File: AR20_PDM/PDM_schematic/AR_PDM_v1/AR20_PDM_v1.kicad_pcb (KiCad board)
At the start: 2 copper layers, 118 x 112 mm, 238 parts, among them J1 S_T_?, J2 1-776163-1, K1 DIPxx-1Cxx-51x, K2 DIPxx-1Cxx-51x, P1 B4B-PH-SM4-TB, Q1 BTS50025-1TAD, Q10 N_FET, Q11 N_FET, Q12 N_FET, Q13 N_FET, Q14 N_FET, Q15 N_FET, Q16 N_FET, Q17 N_FET, Q18 N_FET, Q2 BTS50025-1TAD, Q3 BTS50025-1TAD, Q4 N_FET, Q5 BTS50025-1TAD, Q6 BTS50025-1TAD, Q7 BTS50025-1TAD, Q8 BTS50025-1TAD, Q9 N_FET, SW1 SW_DIP_x07, U1 ACM_2020, U10 Fet-P, U11 Fet-P, U12 Fet-P, U13 Fet-P, U14 Fet-P, U15 Fet-P, U16 Fet-P, U17 Fet-P, U18 Fet-P, U19 Fet-P, U2 INA233, U20 Fet-P, U21 Fet-P, U22 Fet-P, U23 Fet-P, U24 Fet-P, U25 Fet-P, U26 Fet-P, U27 Fet-P, U28 Fet-P, U29 INA233, U3 INA233, U30 INA233, U31 INA233, U4 INA233, U5 INA233, U6 INA233, U7 INA233, U8 INA233, U9 TCA6424ARGJR

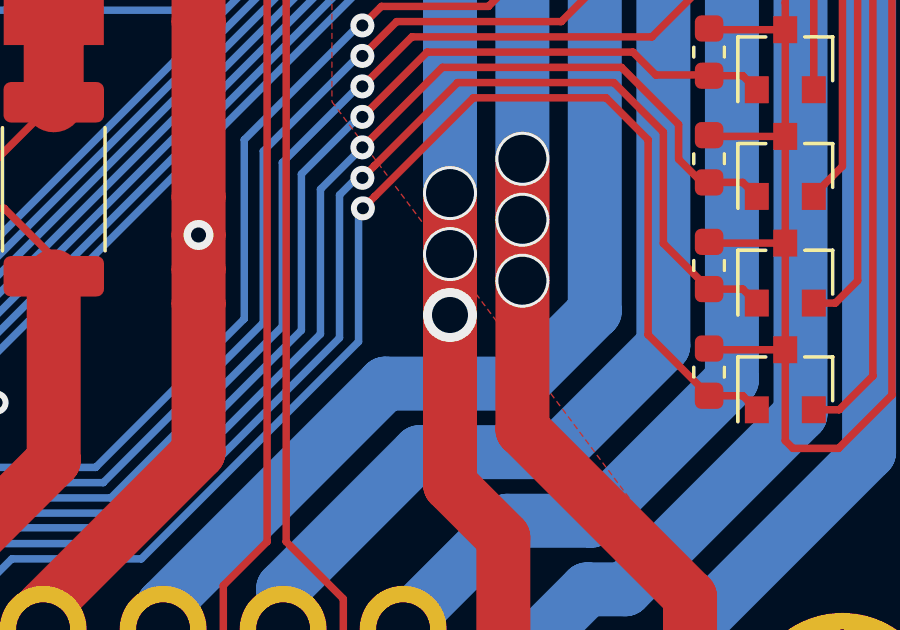
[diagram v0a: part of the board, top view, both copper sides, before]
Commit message: Generated new gerberfile, with forgotten solder mask
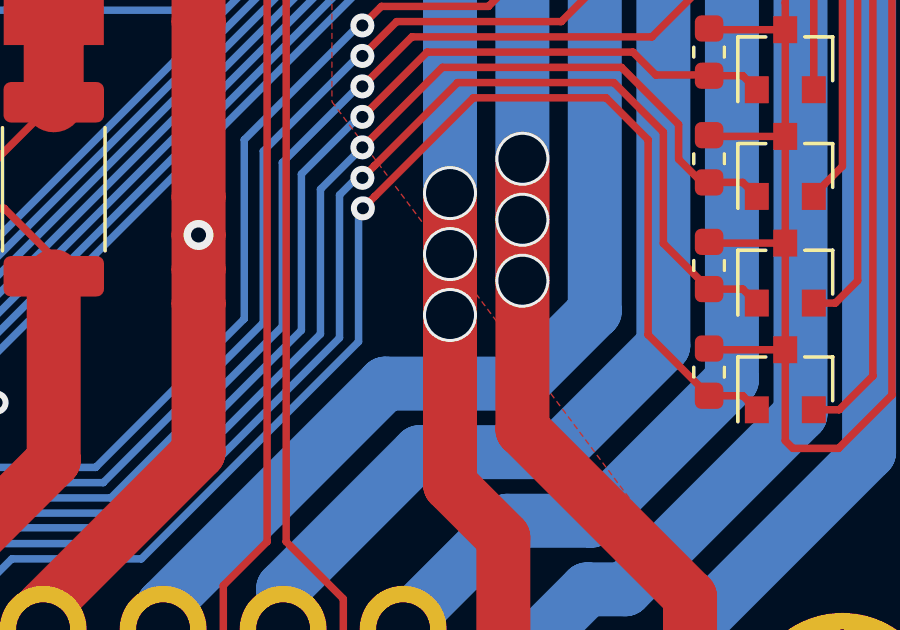
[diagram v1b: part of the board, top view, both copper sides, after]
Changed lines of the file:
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@@
     (visible_elements 7FFFFFFF)
     (pcbplotparams
-      (layerselection 0x0103c_ffffffff)
-      (usegerberextensions false)
+      (layerselection 0x010fc_ffffffff)
+      (usegerberextensions true)
       (usegerberattributes false)
       (usegerberadvancedattributes false)
@@
       (psnegative false)
       (psa4output false)
-      (plotreference false)
-      (plotvalue false)
+      (plotreference true)
+      (plotvalue true)
       (plotinvisibletext false)
       (padsonsilk false)
@@
   (segment (start 131.064 94.594) (end 134.747 98.277) (width 1.8) (layer B.Cu) (net 63))
   (segment (start 134.747 119.634) (end 134.747 124.206) (width 1.8) (layer B.Cu) (net 63))
-  (via (at 134.747 124.206) (size 1.8) (drill 1.2) (layers F.Cu B.Cu) (net 63) (status 1000000))
+  (via (at 134.747 124.206) (size 1.8) (drill 1.6) (layers F.Cu B.Cu) (net 63) (status 1000000))
   (segment (start 138.811 146.177) (end 140.97 146.177) (width 1.8) (layer F.Cu) (net 64))
   (via (at 138.811 146.177) (size 1.8) (drill 1.6) (layers F.Cu B.Cu) (net 64))

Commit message: Major redesign. schematics completed, PCB work in progress
-TODO : A proper changelog file. Where all changes will apear 
- Redesigned schematics to accommodate errors in the improvement list
- More detail in ALPHA improvement list
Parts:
- removed Q10, Q11, Q12, Q13, Q14, Q15, Q16, Q17, Q18, Q4, Q9: N_FET, Package_TO_SOT_SMD:SOT-23
- removed the R23 at (58.3, 122.6)
- removed R_s1: 4K7, Resistor_SMD:R_0603_1608Metric
- added C47: 100nf, Capacitor_SMD:C_0603_1608Metric, F.Cu at (220.2, 49.7)
- added D32: 15V, AR_PDM_v1:Diode-BZX585-C15,115, F.Cu at (214.7, 62.8)
- added D33: 15V, AR_PDM_v1:Diode-BZX585-C15,115, F.Cu at (215.1, 60.2)
- added D34: 15V, AR_PDM_v1:Diode-BZX585-C15,115, F.Cu at (211.1, 62.8)
- added D35: MCU_Feed_Fault, LED_SMD:LED_1206_3216Metric, F.Cu at (185.6, 50.1)
- added D36: ETC_OUT_Fault, LED_SMD:LED_1206_3216Metric, F.Cu at (185.6, 53.5)
- added D37: Shutdown_out_Fault, LED_SMD:LED_1206_3216Metric, F.Cu at (191.3, 50.1)
- added D38: ING_Switch_Fault, LED_SMD:LED_1206_3216Metric, F.Cu at (185.6, 56.9)
- added D39: 15V, AR_PDM_v1:Diode-BZX585-C15,115, F.Cu at (188.5, 65.9)
- added D40: 15V, AR_PDM_v1:Diode-BZX585-C15,115, F.Cu at (188.5, 68.3)
- added IC1: TMUX1208PWR, AR_PDM_v1:TMUX1208PWR, F.Cu at (213.8, 51.8)
- added R100: 4k7, Resistor_SMD:R_0603_1608Metric, F.Cu at (199.3, 56.7)
- added R101: 628R, Resistor_SMD:R_0603_1608Metric, F.Cu at (199.3, 54.2)
- added R102: 4k7, Resistor_SMD:R_0603_1608Metric, F.Cu at (194.9, 58.8)
- added R103: 628R, Resistor_SMD:R_0603_1608Metric, F.Cu at (184.8, 59.8)
- added R104: 4k7, Resistor_SMD:R_0603_1608Metric, F.Cu at (184.8, 68.4)
- added R105: 4k7, Resistor_SMD:R_0603_1608Metric, F.Cu at (184.8, 65.9)
- added R23 (x2): 4k7, Resistor_SMD:R_0603_1608Metric, F.Cu at (58.3, 118.5)
- added R95: 4k7, Resistor_SMD:R_0603_1608Metric, F.Cu at (211.3, 60.3)
- added R96: 4k7, Resistor_SMD:R_0603_1608Metric, F.Cu at (203.3, 56.7)
- added R97: 628R, Resistor_SMD:R_0603_1608Metric, F.Cu at (202.9, 59.2)
- added R98: 4k7, Resistor_SMD:R_0603_1608Metric, F.Cu at (198.9, 59.2)
- added R99: 628R, Resistor_SMD:R_0603_1608Metric, F.Cu at (203.3, 54.2)
- added U32: Fet-P, AR_PDM_v1:P-MOS-BSS83PH6327XTSA1, F.Cu at (196.3, 50.7)
- added U33: Fet-P, AR_PDM_v1:P-MOS-BSS83PH6327XTSA1, F.Cu at (190.6, 58.6)
- added U34: Fet-P, AR_PDM_v1:P-MOS-BSS83PH6327XTSA1, F.Cu at (195.1, 55.2)
- added U35: Fet-P, AR_PDM_v1:P-MOS-BSS83PH6327XTSA1, F.Cu at (200.7, 50.7)
- added U36: Fet-P, AR_PDM_v1:P-MOS-BSS83PH6327XTSA1, F.Cu at (190.6, 54.1)
- C13, C18, C23, C28, C33, C38, C8: value 10nf -> 10nf 50Volt
- D26: value MCU_FEED_Fault -> 15V; footprint LED_SMD:LED_1206_3216Metric -> AR_PDM_v1:Diode-BZX585-C15,115
- D27: value ETC_Fault -> 15V; footprint LED_SMD:LED_1206_3216Metric -> AR_PDM_v1:Diode-BZX585-C15,115
- D28: value Shutdown_OUT_Fault -> 15V; footprint LED_SMD:LED_1206_3216Metric -> AR_PDM_v1:Diode-BZX585-C15,115
- D29: value IGN_Fault -> 15V; footprint LED_SMD:LED_1206_3216Metric -> AR_PDM_v1:Diode-BZX585-C15,115
- R11, R15, R20, R24, R28, R32, R7: footprint Resistor_SMD:R_0603_1608Metric -> Resistor_SMD:R_2512_6332Metric
- R34, R35, R36, R37, R38, R39: value 4K7 -> 4k7
- R5: value 4k7 -> 4K7
- R79, R81, R85, R87: value 628R -> 4k7
- SW1: footprint AR_PDM_v1:DIPSwitch -> AR_PDM_v1:Dip-Switch-14
- U10, U11, U13, U14: value Fet-P -> N-MOS; footprint Package_TO_SOT_SMD:SOT-23 -> AR_PDM_v1:N-MOS-DMN6140L-13
- U12: value Fet-P -> P-MOS; footprint Package_TO_SOT_SMD:SOT-23 -> AR_PDM_v1:P-MOS-BSS83PH6327XTSA1
- U15, U16, U17, U18, U19, U20, U21, U22, U23, U24, U25, U26, U27, U28: value Fet-P -> NMOS; footprint Package_TO_SOT_SMD:SOT-23 -> AR_PDM_v1:N-MOS-DMN6140L-13
- moved R11 197.2 mm to (264.0, 122.4)
- moved R7 192.3 mm to (235.5, 124.3)
- moved R5 191.5 mm to (239.3, 143.4)
- moved R22 185.9 mm to (242.4, 143.3)
- moved R24 185.9 mm to (240.8, 123.4)
- moved R36 184.5 mm to (260.4, 96.9)
- moved C10 184.5 mm to (229.0, 99.8)
- moved C14 184.5 mm to (254.3, 99.8)
- moved C15 184.5 mm to (252.3, 99.8)
- moved C19 184.5 mm to (277.6, 99.8)
- moved C20 184.5 mm to (275.7, 99.8)
- moved C24 184.5 mm to (289.3, 99.8)
- moved C25 184.5 mm to (287.4, 99.8)
- moved C29 184.5 mm to (242.6, 99.8)
- moved C30 184.5 mm to (240.7, 99.8)
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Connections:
- D21 pad 2: Shutdown_Led -> Shutdown_Relay_Side
- D25 pad 1: Net-(D25-Pad1) -> GND
- D26 pad 2: Net-(D26-Pad2) -> GND
- D27 pad 2: Net-(D27-Pad2) -> GND
- D28 pad 2: Net-(D28-Pad2) -> GND
- D29 pad 2: Net-(D29-Pad2) -> GND
- D30 pad 1: Shutdown_Led -> Shutdown_Relay_Side
- D31 pad 1: Shutdown_Led -> Shutdown_Relay_Side
- K1 pad 6: Shutdown_Led -> Shutdown_Relay_Side
- K2 pad 6: Shutdown_Led -> Shutdown_Relay_Side
- R13 pad 1: vcc_5v -> Net-(D27-Pad1)
- R13 pad 2: P5_MOS_IN -> P2_EN_AUX
- R18 pad 1: vcc_5v -> Net-(D28-Pad1)
- R18 pad 2: P6_MOS_IN -> P3_EN_AUX
- R22 pad 1: vcc_5v -> Net-(D29-Pad1)
- R22 pad 2: P2_MOS_IN -> P4_EN_AUX
- R26 pad 1: vcc_5v -> Net-(D32-Pad1)
- R26 pad 2: P4_MOS_IN -> P5_EN_AUX
- R30 pad 1: vcc_5v -> Net-(D33-Pad1)
- R30 pad 2: P7_MOS_IN -> P6_EN_AUX
- R34 pad 1: GND -> Net-(D34-Pad1)
- R34 pad 2: P1_MOS_SENSE_Select -> P7_EN_AUX
- R35 pad 1: GND -> Net-(D26-Pad1)
- R35 pad 2: P2_MOS_SENSE_Select -> GND
- R36 pad 1: GND -> Net-(D27-Pad1)
- R36 pad 2: P3_MOS_SENSE_Select -> GND
- R37 pad 1: GND -> Net-(D28-Pad1)
- R37 pad 2: P4_MOS_SENSE_Select -> GND
- R38 pad 1: GND -> Net-(D29-Pad1)
- R38 pad 2: P6_MOS_SENSE_Select -> GND
- R39 pad 1: GND -> Net-(D32-Pad1)
- R39 pad 2: P7_MOS_SENSE_Select -> GND
- R42 pad 1: P1_EN_ACM -> Net-(D33-Pad1)
- R43 pad 1: P1_EN_AUX -> Net-(D34-Pad1)
- R48 pad 1: P2_EN_ACM -> Net-(R48-Pad1)
- R48 pad 2: GND -> vcc_5v
- R49 pad 1: P2_EN_AUX -> Net-(R49-Pad1)
- R49 pad 2: GND -> vcc_5v
- R5 pad 1: vcc_5v -> Net-(R5-Pad1)
- R5 pad 2: P1_MOS_IN -> SHUTDOWN_IN
- R56 pad 1: P3_EN_ACM -> Net-(R56-Pad1)
- R56 pad 2: GND -> vcc_5v
- R57 pad 1: P3_EN_AUX -> Net-(R57-Pad1)
- R57 pad 2: GND -> vcc_5v
- R62 pad 1: P4_EN_ACM -> Net-(R62-Pad1)
- R62 pad 2: GND -> vcc_5v
- R63 pad 1: P4_EN_AUX -> Net-(R63-Pad1)
- R63 pad 2: GND -> vcc_5v
- R65 pad 1: P5_EN_ACM -> Net-(R65-Pad1)
- R65 pad 2: GND -> vcc_5v
- R66 pad 1: P5_EN_AUX -> P1_EN_ACM
- R69 pad 1: P6_EN_ACM -> P1_EN_ACM
- R69 pad 2: GND -> P1_MOS_IN
- R70 pad 1: P6_EN_AUX -> P2_EN_ACM
- R72 pad 1: P7_EN_ACM -> P2_EN_ACM
- R72 pad 2: GND -> P2_MOS_IN
- R73 pad 1: P7_EN_AUX -> P3_EN_ACM
- R77 pad 1: V+12V -> Net-(R77-Pad1)
- R78 pad 1: MCU_UNITS_FEED_OUT -> P3_EN_ACM
- R78 pad 2: GND -> P3_MOS_IN
- R79 pad 1: V+12V -> P4_EN_ACM
- R79 pad 2: Net-(D26-Pad2) -> GND
- R80 pad 1: ETC_OUT -> P4_EN_ACM
- R80 pad 2: GND -> P4_MOS_IN
- R81 pad 1: V+12V -> P5_EN_ACM
- R81 pad 2: Net-(D27-Pad2) -> GND
- R83 pad 1: SHUTDOWN_OUT -> P5_EN_ACM
- R83 pad 2: GND -> P5_MOS_IN
- R85 pad 1: V+12V -> P6_EN_ACM
- R85 pad 2: Net-(D28-Pad2) -> GND
- R86 pad 1: IGN_SWITCH_OUT -> P6_EN_ACM
- R86 pad 2: GND -> P6_MOS_IN
- R87 pad 1: V+12V -> P7_EN_ACM
- R87 pad 2: Net-(D29-Pad2) -> GND
- R9 pad 1: vcc_5v -> Net-(D26-Pad1)
- R9 pad 2: P3_MOS_IN -> P1_EN_AUX
- R90 pad 1: FP_ENABLE_ACM -> Net-(D39-Pad1)
- R92 pad 1: FP_ENABLE_AUX -> Net-(D40-Pad1)
- U10 pad 1: P1_EN_ACM -> P6_MOS_IN
- U10 pad 2: P1_MOS_IN -> GND
- U10 pad 3: GND -> P6_GearA_open_drain_output
- U11 pad 1: P1_EN_AUX -> ACM_Shutdown_Circuit
- U11 pad 2: Net-(SW1-Pad1) -> GND
- U11 pad 3: GND -> Net-(R5-Pad1)
- U12 pad 1: P2_EN_ACM -> Net-(R5-Pad1)
- U12 pad 2: P2_MOS_IN -> SHUTDOWN_IN
- U12 pad 3: GND -> Shutdown_Relay_Side
- U13 pad 1: P2_EN_AUX -> Net-(D39-Pad1)
- U13 pad 2: Net-(SW1-Pad2) -> GND
- U13 pad 3: GND -> FP_ENABLE_RELAY_SINK
- U14 pad 1: P3_EN_ACM -> Net-(D40-Pad1)
- U14 pad 2: P3_MOS_IN -> GND
- U14 pad 3: GND -> FP_ENABLE_RELAY_SINK
- U15 pad 1: P3_EN_AUX -> Net-(D26-Pad1)
- U15 pad 2: Net-(SW1-Pad3) -> GND
- U15 pad 3: GND -> Net-(R48-Pad1)
- U16 pad 1: P4_EN_ACM -> Net-(D27-Pad1)
- U16 pad 2: P4_MOS_IN -> GND
- U16 pad 3: GND -> Net-(R49-Pad1)
- U17 pad 1: P4_EN_AUX -> Net-(D28-Pad1)
- U17 pad 2: Net-(SW1-Pad4) -> GND
- U17 pad 3: GND -> Net-(R56-Pad1)
- U18 pad 1: P5_EN_ACM -> Net-(D29-Pad1)
- U18 pad 2: P5_MOS_IN -> GND
- U18 pad 3: GND -> Net-(R57-Pad1)
- U19 pad 1: P5_EN_AUX -> Net-(D32-Pad1)
- U19 pad 2: Net-(SW1-Pad5) -> GND
- U19 pad 3: GND -> Net-(R62-Pad1)
- U2 pad 10: P1_OUT -> P1_Shunt
- U2 pad 8: P1_Shunt -> P1_OUT
- U2 pad 9: P1_Shunt -> P1_OUT
- U20 pad 1: P6_EN_ACM -> Net-(D33-Pad1)
- U20 pad 2: P6_MOS_IN -> GND
- U20 pad 3: GND -> Net-(R63-Pad1)
- U21 pad 1: P6_EN_AUX -> Net-(D34-Pad1)
- U21 pad 2: Net-(SW1-Pad6) -> GND
- U21 pad 3: GND -> Net-(R65-Pad1)
- U22 pad 1: P7_EN_ACM -> Net-(R48-Pad1)
- U22 pad 2: P7_MOS_IN -> GND
- U22 pad 3: GND -> Net-(SW1-Pad1)
- U23 pad 1: P7_EN_AUX -> Net-(R49-Pad1)
- U23 pad 2: Net-(SW1-Pad7) -> GND
- U23 pad 3: GND -> Net-(SW1-Pad2)
- U24 pad 1: CLUTCH_ACT_OUT -> Net-(R56-Pad1)
- U24 pad 2: Net-(D25-Pad1) -> GND
- U24 pad 3: GND -> Net-(SW1-Pad3)
- U25 pad 1: MCU_UNITS_FEED_OUT -> Net-(R57-Pad1)
- U25 pad 2: Net-(D26-Pad1) -> GND
- U25 pad 3: GND -> Net-(SW1-Pad4)
- U26 pad 1: ETC_OUT -> Net-(R62-Pad1)
- U26 pad 2: Net-(D27-Pad1) -> GND
- U26 pad 3: GND -> Net-(SW1-Pad5)
- U27 pad 1: SHUTDOWN_OUT -> Net-(R63-Pad1)
- U27 pad 2: Net-(D28-Pad1) -> GND
- U27 pad 3: GND -> Net-(SW1-Pad6)
- U28 pad 1: IGN_SWITCH_OUT -> Net-(R65-Pad1)
- U28 pad 2: Net-(D29-Pad1) -> GND
- U28 pad 3: GND -> Net-(SW1-Pad7)
- U29 pad 3: COIL_INJECTOR_Alert -> /Fuel_Ignition_ShutdownCircuit/COIL_INJECTOR_Alert
- U29 pad 8: Net-(F_COIL1-Pad2) -> Net-(K1-Pad14)
- U3 pad 10: P3_OUT -> P3_Shunt
- U3 pad 8: P3_Shunt -> P3_OUT
- U3 pad 9: P3_Shunt -> P3_OUT
- U30 pad 3: FP_Alert -> /Fuel_Ignition_ShutdownCircuit/FP_Alert
- U30 pad 8: Net-(F_FP1-Pad2) -> Net-(K2-Pad14)
- U31 pad 8: V+12V -> Net-(F1-Pad2)
- U4 pad 10: P5_OUT -> P5_Shunt
- U4 pad 8: P5_Shunt -> P5_OUT
- U4 pad 9: P5_Shunt -> P5_OUT
- U5 pad 10: P6_OUT -> P6_Shunt
- U5 pad 8: P6_Shunt -> P6_OUT
- U5 pad 9: P6_Shunt -> P6_OUT
- U6 pad 10: P2_OUT -> P2_Shunt
- U6 pad 8: P2_Shunt -> P2_OUT
- U6 pad 9: P2_Shunt -> P2_OUT
- U7 pad 10: P4_OUT -> P4_Shunt
- U7 pad 8: P4_Shunt -> P4_OUT
- U7 pad 9: P4_Shunt -> P4_OUT
- U8 pad 10: P7_OUT -> P7_Shunt
- U8 pad 8: P7_Shunt -> P7_OUT
- U8 pad 9: P7_Shunt -> P7_OUT
- U9 pad 10: P1_MOS_SENSE_Select -> Mux_select_A1
- U9 pad 11: P2_MOS_SENSE_Select -> Mux_select_A1
- U9 pad 12: P3_MOS_SENSE_Select -> Mux_select_A0
- U9 pad 13: P4_MOS_SENSE_Select -> Mux_enable
- U9 pad 14: P5_MOS_SENSE_Select -> Net-(U9-Pad14)
- U9 pad 15: P6_MOS_SENSE_Select -> Net-(U9-Pad15)
- U9 pad 16: P7_MOS_SENSE_Select -> Net-(U9-Pad16)
- U9 pad 17: FP_Alert -> Net-(U9-Pad17)
- U9 pad 18: COIL_INJECTOR_Alert -> Net-(U9-Pad18)
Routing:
- net GND: track 1109.1 -> 863.4 mm, vias 63 -> 50
- net MOS_SENSE_ALL: track 235.1 -> 3.83 mm, vias 7 -> 0
- net Shutdown_Led: track 222.3 -> 0.00 mm, vias 2 -> 0
- net Shutdown_Relay_Side: track 0.00 -> 222.0 mm, vias 0 -> 2
- net SLC: track 402.2 -> 235.8 mm, vias 17 -> 13
- net SDA: track 390.3 -> 230.0 mm, vias 15 -> 12
- net CAN_HIGH: track 112.2 -> 0.00 mm, vias 2 -> 0
- net CAN_LOW: track 112.2 -> 0.28 mm, vias 2 -> 0
- net V+12V: track 127.6 -> 44.1 mm, vias 10 -> 3
- net P1_MOS_SENSE_Select: track 75.5 -> 0.00 mm, vias 1 -> 0
- net FUEL_PUMP_Fault: track 72.8 -> 2.22 mm, vias 2 -> 1
- net COIL_INJECTOR_Fault: track 73.3 -> 6.03 mm, vias 2 -> 1
- net FP_Alert: track 65.4 -> 0.00 mm, vias 2 -> 0
- net Net-(D26-Pad1): track 63.6 -> 0.00 mm, vias 2 -> 0
- net Net-(D27-Pad1): track 61.5 -> 0.00 mm, vias 2 -> 0
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- removed copper zone on B.Cu, net V+12V

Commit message: All components in place - PCB work in progress
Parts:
- removed the R23 at (58.3, 118.5)
- C47, D26, D27, D28, D29, D32, D33, D34, D39, D40, IC1, R101, R103, R104, R105, R43, R66, R70, R73, R74, R75, R77, R78, R79, R80, R81, R83, R85, R86, R87, R95, R97, R99, U11, U13, U15, U17, U19, U21: moved to B.Cu
- R48, R56, R62, R65, U22: moved to F.Cu
- moved U12 196.7 mm to (74.8, 140.6), turned to 90 degrees
- moved R39 194.5 mm to (114.6, 129.5), turned to 270 degrees
- moved R11 192.0 mm to (73.3, 100.2), turned to 180 degrees
- moved R38 188.2 mm to (110.0, 129.5), turned to 270 degrees
- moved U14 187.9 mm to (79.5, 132.6)
- moved C29 186.6 mm to (55.9, 100.4)
- moved R7 186.6 mm to (50.5, 100.1), turned to 180 degrees
- moved C14 186.5 mm to (67.8, 100.5)
- moved C24 186.4 mm to (102.9, 100.5)
- moved C39 186.4 mm to (114.6, 100.4)
- moved C34 186.2 mm to (79.7, 100.5)
- moved C19 186.2 mm to (91.4, 100.5)
- moved C9 185.8 mm to (45.1, 100.4)
- moved R24 180.9 mm to (61.4, 100.2), turned to 180 degrees
- moved C30 180.8 mm to (59.9, 103.4), turned to 180 degrees
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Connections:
- IC1 pad 10: P7_MOS_SENSE -> P1_MOS_SENSE
- IC1 pad 11: P6_MOS_SENSE -> P2_MOS_SENSE
- IC1 pad 12: P5_MOS_SENSE -> P3_MOS_SENSE
- IC1 pad 15: Mux_select_A1 -> Mux_select_A2
- IC1 pad 3: Net-(IC1-Pad3) -> (no net)
- IC1 pad 4: P1_MOS_SENSE -> P7_MOS_SENSE
- IC1 pad 5: P2_MOS_SENSE -> P6_MOS_SENSE
- IC1 pad 6: P3_MOS_SENSE -> P5_MOS_SENSE
- IC1 pad 9: Net-(IC1-Pad9) -> (no net)
- J2 pad 31: Net-(J2-Pad31) -> (no net)
- J2 pad 32: Net-(J2-Pad32) -> (no net)
- K1 pad 1: Net-(K1-Pad1) -> (no net)
- K2 pad 1: Net-(K2-Pad1) -> (no net)
- Q1 pad 4: Net-(Q1-Pad4) -> (no net)
- Q2 pad 4: Net-(Q2-Pad4) -> (no net)
- Q3 pad 4: Net-(Q3-Pad4) -> (no net)
- Q5 pad 4: Net-(Q5-Pad4) -> (no net)
- Q6 pad 4: Net-(Q6-Pad4) -> (no net)
- Q7 pad 4: Net-(Q7-Pad4) -> (no net)
- Q8 pad 4: Net-(Q8-Pad4) -> (no net)
- SW1 pad 12: P3_MOS_IN -> (no net)
- U1 pad 10: Net-(U1-Pad10) -> (no net)
- U1 pad 11: Net-(U1-Pad11) -> (no net)
- U1 pad 13: Net-(U1-Pad13) -> (no net)
- U1 pad 15: Net-(U1-Pad15) -> (no net)
- U1 pad 19: Net-(U1-Pad19) -> (no net)
- U1 pad 21: Net-(U1-Pad21) -> (no net)
- U1 pad 7: Net-(U1-Pad7) -> (no net)
- U1 pad 9: Net-(U1-Pad9) -> (no net)
- U29 pad 3: /Fuel_Ignition_ShutdownCircuit/COIL_INJECTOR_Alert -> (no net)
- U30 pad 3: /Fuel_Ignition_ShutdownCircuit/FP_Alert -> (no net)
- U31 pad 3: /Fuses_Direct/DIRECT_Alert -> (no net)
- U9 pad 10: Mux_select_A1 -> Mux_select_A2
- U9 pad 14: Net-(U9-Pad14) -> (no net)
- U9 pad 15: Net-(U9-Pad15) -> (no net)
- U9 pad 16: Net-(U9-Pad16) -> (no net)
- U9 pad 17: Net-(U9-Pad17) -> (no net)
- U9 pad 18: Net-(U9-Pad18) -> (no net)
- U9 pad 19: Net-(U9-Pad19) -> (no net)
- U9 pad 21: Net-(U9-Pad21) -> (no net)
- U9 pad 22: Net-(U9-Pad22) -> (no net)
- U9 pad 23: Net-(U9-Pad23) -> (no net)
- U9 pad 24: Net-(U9-Pad24) -> (no net)
- U9 pad 33: Net-(U9-Pad33) -> (no net)
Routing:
- net P1_Shunt: track 54.4 -> 198.8 mm
- net P2_Shunt: track 56.8 -> 189.3 mm
- net CAN_HIGH: track 0.00 -> 119.8 mm, vias 0 -> 2
- net CAN_LOW: track 0.28 -> 118.8 mm, vias 0 -> 2
- net P3_Shunt: track 63.0 -> 179.0 mm
- net P7_MOS_SENSE: track 10.6 -> 125.2 mm
- net P4_Shunt: track 61.3 -> 168.8 mm
- net P6_MOS_SENSE: track 9.21 -> 114.6 mm
- net V+12V: track 44.1 -> 146.0 mm, vias 3 -> 14
- net P5_Shunt: track 63.2 -> 158.6 mm
- net P5_MOS_SENSE: track 12.4 -> 104.3 mm
- net P6_Shunt: track 65.5 -> 147.7 mm
- net P4_MOS_SENSE: track 12.3 -> 93.8 mm
- net P3_MOS_SENSE: track 12.3 -> 90.7 mm
- net P7_Shunt: track 67.0 -> 138.8 mm
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- removed copper zone on F.Cu, net GND
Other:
- board text added: "Clutch"
- board text added: "ETC"
- board text added: "FUSES"
- board text added: "Fuel ACM"
- board text added: "Fuel AUX"
- board text added: "Ignition"
- board text added: "MCU"
- board text added: "Pico SD"
- board text added: "Shutdn"

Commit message: Pdm version B Draft finished
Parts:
- moved IC1 15.8 mm to (71.3, 58.9)
- moved C47 15.7 mm to (77.2, 59.4), turned to 270 degrees
- moved U11 15.0 mm to (71.6, 128.8)
- moved R89 15.0 mm to (71.8, 126.1)
- moved U12 13.4 mm to (75.1, 127.2), turned to 0 degrees
- moved R5 13.4 mm to (74.9, 129.8), turned to 0 degrees
- moved D30 11.6 mm to (56.1, 131.4), turned to 90 degrees
- moved D31 10.3 mm to (54.4, 131.4), turned to 90 degrees
- moved U14 4.79 mm to (84.0, 130.9)
- moved R92 4.66 mm to (84.0, 128.4)
- moved R105 4.64 mm to (84.0, 125.3)
- moved D40 4.61 mm to (84.0, 126.8)
- moved D39 4.30 mm to (79.8, 126.8)
- moved U13 4.23 mm to (79.7, 130.9)
- moved R90 4.21 mm to (79.8, 128.4)
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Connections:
- IC1 pad 3: (no net) -> Net-(IC1-Pad3)
- IC1 pad 9: (no net) -> Net-(IC1-Pad9)
- J2 pad 31: (no net) -> Net-(J2-Pad31)
- J2 pad 32: (no net) -> Net-(J2-Pad32)
- K1 pad 1: (no net) -> Net-(K1-Pad1)
- K2 pad 1: (no net) -> Net-(K2-Pad1)
- Q1 pad 4: (no net) -> Net-(Q1-Pad4)
- Q2 pad 4: (no net) -> Net-(Q2-Pad4)
- Q3 pad 4: (no net) -> Net-(Q3-Pad4)
- Q5 pad 4: (no net) -> Net-(Q5-Pad4)
- Q6 pad 4: (no net) -> Net-(Q6-Pad4)
- Q7 pad 4: (no net) -> Net-(Q7-Pad4)
- Q8 pad 4: (no net) -> Net-(Q8-Pad4)
- SW1 pad 12: (no net) -> P3_MOS_IN
- U1 pad 10: (no net) -> Net-(U1-Pad10)
- U1 pad 11: (no net) -> Net-(U1-Pad11)
- U1 pad 13: (no net) -> Net-(U1-Pad13)
- U1 pad 15: (no net) -> Net-(U1-Pad15)
- U1 pad 19: (no net) -> Net-(U1-Pad19)
- U1 pad 21: (no net) -> Net-(U1-Pad21)
- U1 pad 7: (no net) -> Net-(U1-Pad7)
- U1 pad 9: (no net) -> Net-(U1-Pad9)
- U29 pad 3: (no net) -> /Fuel_Ignition_ShutdownCircuit/COIL_INJECTOR_Alert
- U30 pad 3: (no net) -> /Fuel_Ignition_ShutdownCircuit/FP_Alert
- U31 pad 3: (no net) -> /Fuses_Direct/DIRECT_Alert
- U9 pad 14: (no net) -> Net-(U9-Pad14)
- U9 pad 15: (no net) -> Net-(U9-Pad15)
- U9 pad 16: (no net) -> Net-(U9-Pad16)
- U9 pad 17: (no net) -> Net-(U9-Pad17)
- U9 pad 18: (no net) -> Net-(U9-Pad18)
- U9 pad 19: (no net) -> Net-(U9-Pad19)
- U9 pad 21: (no net) -> Net-(U9-Pad21)
- U9 pad 22: (no net) -> Net-(U9-Pad22)
- U9 pad 23: (no net) -> Net-(U9-Pad23)
- U9 pad 24: (no net) -> Net-(U9-Pad24)
- U9 pad 33: (no net) -> Net-(U9-Pad33)
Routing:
- net GND: track 842.3 -> 961.9 mm, vias 56 -> 64
- net P7_MOS_SENSE: track 125.2 -> 147.7 mm
- net P6_MOS_SENSE: track 114.6 -> 137.0 mm
- net P5_MOS_SENSE: track 104.3 -> 126.5 mm
- net P4_MOS_SENSE: track 93.8 -> 115.7 mm
- net P3_MOS_SENSE: track 90.7 -> 112.4 mm
- net P2_MOS_SENSE: track 80.4 -> 101.4 mm
- net Net-(R2-Pad1): track 5.52 -> 25.1 mm, vias 1 -> 2
- net Net-(K1-Pad14): track 128.1 -> 146.6 mm
- net Shutdown_Relay_Side: track 228.1 -> 212.4 mm
- net P1_MOS_SENSE: track 75.5 -> 90.5 mm
- net FUEL_PUMP_OUT: track 227.8 -> 213.4 mm, vias 1 -> 2
- net Net-(K2-Pad14): track 159.8 -> 173.3 mm
- net TX: track 183.3 -> 192.8 mm
- net ACM_Shutdown_Circuit: track 168.1 -> 158.6 mm, vias 3 -> 1
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- added copper zone on F.Cu, net GND
- added copper zone on B.Cu, net V+12V
